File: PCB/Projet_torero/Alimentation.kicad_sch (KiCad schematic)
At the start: 21 parts, among them IC501 MP1475SGJ-P, J202 Conn_02x02_Odd_Even, J501 Conn_01x02, U501 BU33SD5WG-TR

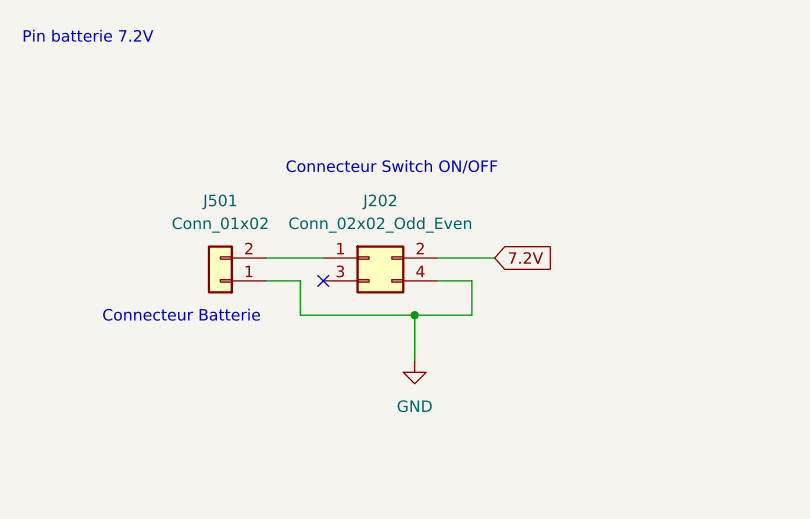
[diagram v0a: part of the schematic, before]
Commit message: Ajout Switch ON/OFF sur carte
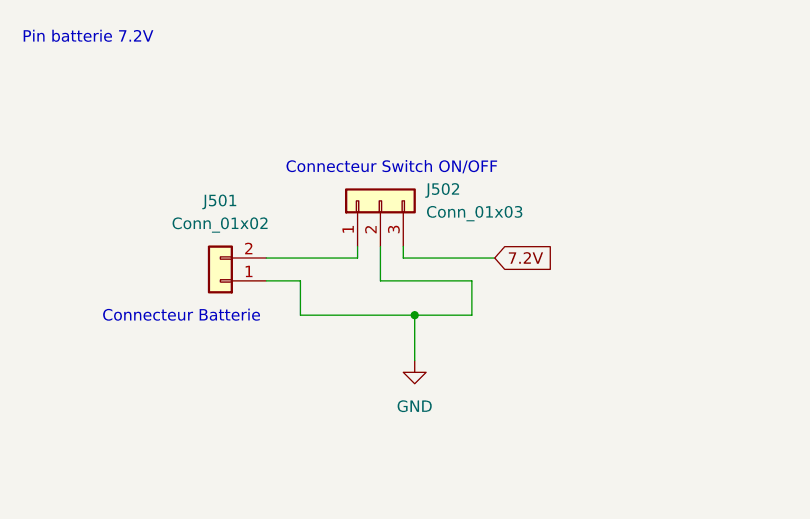
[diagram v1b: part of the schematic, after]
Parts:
- removed J202: Conn_02x02_Odd_Even, symbol Connector_Generic:Conn_02x02_Odd_Even
- added J502: Conn_01x03, symbol Connector_Generic:Conn_01x03
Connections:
- net 7.2V: now also J502.3 (Pin_3)
- net GND: now also J502.2 (Pin_2)
- net at J501.2 (Pin_2): now also J502.1 (Pin_1)
- no-connect marks 1 -> 0
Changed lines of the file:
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@@
 		(color 0 0 0 0)
 	)
-	(no_connect
-		(at 46.99 40.64)
-	)
 	(polyline
 		(pts
@@
 	(wire
 		(pts
+			(xy 50.8 38.1) (xy 50.8 36.83)
+		)
+		(stroke
+			(width 0)
+			(type default)
+		)
+	)
+	(wire
+		(pts
 			(xy 127 156.21) (xy 127 161.29)
 		)
@@
 	(wire
 		(pts
-			(xy 59.69 40.64) (xy 63.5 40.64)
-		)
-		(stroke
-			(width 0)
-			(type default)
-		)
-	)
-	(wire
-		(pts
-			(xy 59.69 38.1) (xy 66.04 38.1)
-		)
-		(stroke
-			(width 0)
-			(type default)
-		)
-	)
-	(wire
-		(pts
 			(xy 115.57 153.67) (xy 115.57 156.21)
 		)
@@
 	(wire
 		(pts
-			(xy 40.64 38.1) (xy 46.99 38.1)
+			(xy 40.64 38.1) (xy 50.8 38.1)
 		)
 		(stroke
@@
 	(wire
 		(pts
+			(xy 53.34 40.64) (xy 63.5 40.64)
+		)
+		(stroke
+			(width 0)
+			(type default)
+		)
+	)
+	(wire
+		(pts
 			(xy 205.74 123.19) (xy 207.01 123.19)
 		)
@@
 		)
 	)
+	(wire
+		(pts
+			(xy 55.88 38.1) (xy 66.04 38.1)
+		)
+		(stroke
+			(width 0)
+			(type default)
+		)
+	)
 	(polyline
 		(pts
@@
 	(wire
 		(pts
+			(xy 55.88 36.83) (xy 55.88 38.1)
+		)
+		(stroke
+			(width 0)
+			(type default)
+		)
+	)
+	(wire
+		(pts
 			(xy 71.12 147.32) (xy 71.12 152.4)
+		)
+		(stroke
+			(width 0)
+			(type default)
+		)
+	)
+	(wire
+		(pts
+			(xy 53.34 36.83) (xy 53.34 40.64)
 		)
 		(stroke
@@
 	)
 	(symbol
-		(lib_id "Connector_Generic:Conn_02x02_Odd_Even")
-		(at 52.07 38.1 0)
+		(lib_id "Connector_Generic:Conn_01x03")
+		(at 53.34 31.75 90)
 		(unit 1)
 		(exclude_from_sim no)
@@
 		(dnp no)
 		(fields_autoplaced yes)
-		(property "Reference" "J202"
+		(property "Reference" "J502"
+			(at 58.42 30.4799 90)
+			(effects
+				(font
+					(size 1.27 1.27)
+				)
+				(justify right)
+			)
+		)
+		(property "Value" "Conn_01x03"
+			(at 58.42 33.0199 90)
+			(effects
+				(font
+					(size 1.27 1.27)
+				)
+				(justify right)
+			)
+		)
+		(property "Footprint" ""
 			(at 53.34 31.75 0)
 			(effects
@@
 					(size 1.27 1.27)
 				)
-			)
-		)
-		(property "Value" "Conn_02x02_Odd_Even"
-			(at 53.34 34.29 0)
-			(effects
-				(font
-					(size 1.27 1.27)
-				)
-			)
-		)
-		(property "Footprint" ""
-			(at 52.07 38.1 0)
-			(effects
-				(font
-					(size 1.27 1.27)
-				)
 				(hide yes)
 			)
 		)
 		(property "Datasheet" "~"
-			(at 52.07 38.1 0)
-			(effects
-				(font
-					(size 1.27 1.27)
-				)
-				(hide yes)
-			)
-		)
-		(property "Description" "Generic connector, double row, 02x02, odd/even pin numbering scheme (row 1 odd numbers, row 2 even numbers), script generated (kicad-library-utils/schlib/autogen/connector/)"
-			(at 52.07 38.1 0)
-			(effects
-				(font
-					(size 1.27 1.27)
-				)
-				(hide yes)
-			)
+			(at 53.34 31.75 0)
+			(effects
+				(font
+					(size 1.27 1.27)
+				)
+				(hide yes)
+			)
+		)
+		(property "Description" "Generic connector, single row, 01x03, script generated (kicad-library-utils/schlib/autogen/connector/)"
+			(at 53.34 31.75 0)
+			(effects
+				(font
+					(size 1.27 1.27)
+				)
+				(hide yes)
+			)
+		)
+		(pin "1"
+		)
+		(pin "2"
 		)
 		(pin "3"
-		)
-		(pin "4"
-		)
-		(pin "2"
-		)
-		(pin "1"
 		)
 		(instances
 			(project ""
 				(path "/04e1eb47-a2c4-462b-bef7-377d9515a2c0/b3b2826c-2e3c-42fe-bcd6-22fcd6249c25"
-					(reference "J202")
+					(reference "J502")
 					(unit 1)
 				)

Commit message: Nouvelle version avec Empreinte correcte
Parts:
- J502: footprint (none) -> Connector_JST:JST_XH_S3B-XH-A_1x03_P2.50mm_Horizontal
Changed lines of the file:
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@@
 			)
 		)
-		(property "Footprint" ""
+		(property "Footprint" "Connector_JST:JST_XH_S3B-XH-A_1x03_P2.50mm_Horizontal"
 			(at 53.34 31.75 0)
 			(effects

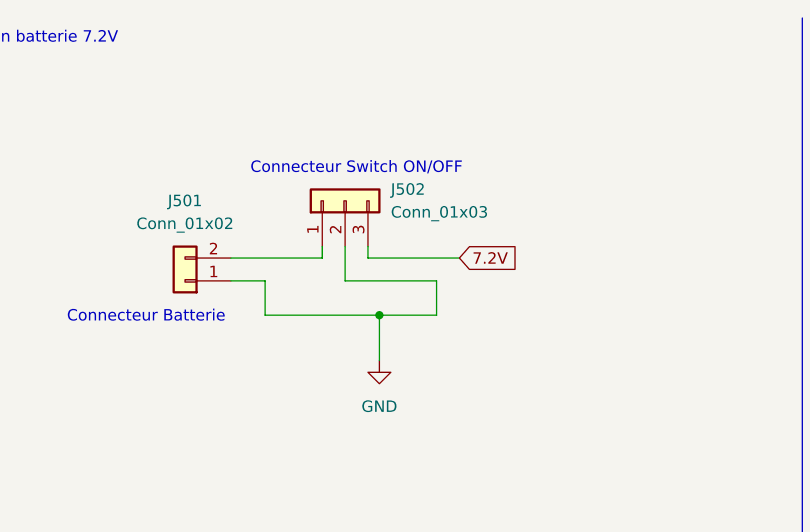
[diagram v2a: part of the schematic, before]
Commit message: Placement des composant "terminé"
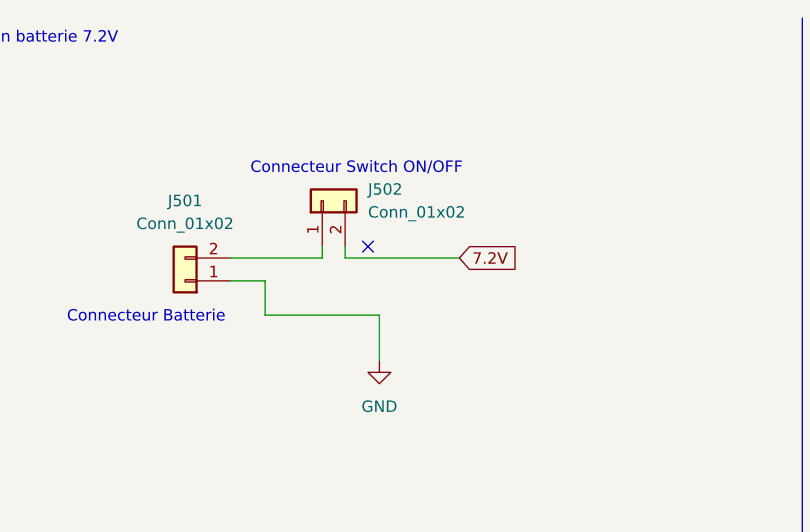
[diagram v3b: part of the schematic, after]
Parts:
- removed J502: Conn_01x03, Connector_JST:JST_XH_S3B-XH-A_1x03_P2.50mm_Horizontal, symbol Connector_Generic:Conn_01x03
- added J502: Conn_01x02, Connector_JST:JST_XH_S2B-XH-A_1x02_P2.50mm_Horizontal, symbol Connector_Generic:Conn_01x02
- C501: footprint Capacitor_SMD:C_0805_2012Metric_Pad1.18x1.45mm_HandSolder -> Capacitor_SMD:C_0805_2012Metric
- C504: footprint Capacitor_SMD:C_0603_1608Metric_Pad1.08x0.95mm_HandSolder -> Capacitor_SMD:C_0603_1608Metric
- L501: footprint Inductor_SMD:L_0603_1608Metric_Pad1.05x0.95mm_HandSolder -> Inductor_SMD:L_Wuerth_WE-TPC-3816
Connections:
- net 7.2V: now also J502.2 (Pin_2)
- net at J501.2 (Pin_2): now also J502.1 (Pin_1)
- no-connect marks 0 -> 1
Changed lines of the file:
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@@
 		(color 0 0 0 0)
 	)
-	(junction
-		(at 57.15 44.45)
-		(diameter 0)
-		(color 0 0 0 0)
+	(no_connect
+		(at 55.88 36.83)
+	)
+	(wire
+		(pts
+			(xy 66.04 38.1) (xy 53.34 38.1)
+		)
+		(stroke
+			(width 0)
+			(type default)
+		)
 	)
 	(polyline
@@
 	(wire
 		(pts
-			(xy 63.5 40.64) (xy 63.5 44.45)
-		)
-		(stroke
-			(width 0)
-			(type default)
-		)
-	)
-	(wire
-		(pts
 			(xy 203.2 120.65) (xy 203.2 127)
 		)
@@
 	(wire
 		(pts
-			(xy 63.5 44.45) (xy 57.15 44.45)
+			(xy 53.34 38.1) (xy 53.34 36.83)
 		)
 		(stroke
@@
 	(wire
 		(pts
-			(xy 53.34 40.64) (xy 63.5 40.64)
-		)
-		(stroke
-			(width 0)
-			(type default)
-		)
-	)
-	(wire
-		(pts
 			(xy 205.74 123.19) (xy 207.01 123.19)
 		)
@@
 		)
 	)
-	(wire
-		(pts
-			(xy 55.88 38.1) (xy 66.04 38.1)
-		)
-		(stroke
-			(width 0)
-			(type default)
-		)
-	)
 	(polyline
 		(pts
@@
 	(wire
 		(pts
-			(xy 55.88 36.83) (xy 55.88 38.1)
-		)
-		(stroke
-			(width 0)
-			(type default)
-		)
-	)
-	(wire
-		(pts
 			(xy 71.12 147.32) (xy 71.12 152.4)
-		)
-		(stroke
-			(width 0)
-			(type default)
-		)
-	)
-	(wire
-		(pts
-			(xy 53.34 36.83) (xy 53.34 40.64)
 		)
 		(stroke
@@
 			)
 		)
-		(property "Footprint" "Capacitor_SMD:C_0805_2012Metric_Pad1.18x1.45mm_HandSolder"
+		(property "Footprint" "Capacitor_SMD:C_0805_2012Metric"
 			(at 46.99 148.59 0)
 			(effects
@@
 			)
 		)
-		(property "Footprint" "Inductor_SMD:L_0603_1608Metric_Pad1.05x0.95mm_HandSolder"
+		(property "Footprint" "Inductor_SMD:L_Wuerth_WE-TPC-3816"
 			(at 110.49 138.43 0)
 			(effects
@@
 	)
 	(symbol
-		(lib_id "Connector_Generic:Conn_01x03")
-		(at 53.34 31.75 90)
-		(unit 1)
-		(exclude_from_sim no)
-		(in_bom yes)
-		(on_board yes)
-		(dnp no)
-		(fields_autoplaced yes)
-		(property "Reference" "J502"
-			(at 58.42 30.4799 90)
-			(effects
-				(font
-					(size 1.27 1.27)
-				)
-				(justify right)
-			)
-		)
-		(property "Value" "Conn_01x03"
-			(at 58.42 33.0199 90)
-			(effects
-				(font
-					(size 1.27 1.27)
-				)
-				(justify right)
-			)
-		)
-		(property "Footprint" "Connector_JST:JST_XH_S3B-XH-A_1x03_P2.50mm_Horizontal"
-			(at 53.34 31.75 0)
-			(effects
-				(font
-					(size 1.27 1.27)
-				)
-				(hide yes)
-			)
-		)
-		(property "Datasheet" "~"
-			(at 53.34 31.75 0)
-			(effects
-				(font
-					(size 1.27 1.27)
-				)
-				(hide yes)
-			)
-		)
-		(property "Description" "Generic connector, single row, 01x03, script generated (kicad-library-utils/schlib/autogen/connector/)"
-			(at 53.34 31.75 0)
-			(effects
-				(font
-					(size 1.27 1.27)
-				)
-				(hide yes)
-			)
-		)
-		(pin "1"
-		)
-		(pin "2"
-		)
-		(pin "3"
-		)
-		(instances
-			(project ""
-				(path "/04e1eb47-a2c4-462b-bef7-377d9515a2c0/b3b2826c-2e3c-42fe-bcd6-22fcd6249c25"
-					(reference "J502")
-					(unit 1)
-				)
-			)
-		)
-	)
-	(symbol
 		(lib_id "power:GND")
 		(at 57.15 49.53 0)
@@
 	)
 	(symbol
+		(lib_id "Connector_Generic:Conn_01x02")
+		(at 50.8 31.75 90)
+		(unit 1)
+		(exclude_from_sim no)
+		(in_bom yes)
+		(on_board yes)
+		(dnp no)
+		(fields_autoplaced yes)
+		(property "Reference" "J502"
+			(at 55.88 30.4799 90)
+			(effects
+				(font
+					(size 1.27 1.27)
+				)
+				(justify right)
+			)
+		)
+		(property "Value" "Conn_01x02"
+			(at 55.88 33.0199 90)
+			(effects
+				(font
+					(size 1.27 1.27)
+				)
+				(justify right)
+			)
+		)
+		(property "Footprint" "Connector_JST:JST_XH_S2B-XH-A_1x02_P2.50mm_Horizontal"
+			(at 50.8 31.75 0)
+			(effects
+				(font
+					(size 1.27 1.27)
+				)
+				(hide yes)
+			)
+		)
+		(property "Datasheet" "~"
+			(at 50.8 31.75 0)
+			(effects
+				(font
+					(size 1.27 1.27)
+				)
+				(hide yes)
+			)
+		)
+		(property "Description" "Generic connector, single row, 01x02, script generated (kicad-library-utils/schlib/autogen/connector/)"
+			(at 50.8 31.75 0)
+			(effects
+				(font
+					(size 1.27 1.27)
+				)
+				(hide yes)
+			)
+		)
+		(pin "1"
+		)
+		(pin "2"
+		)
+		(instances
+			(project "Projet_torero"
+				(path "/04e1eb47-a2c4-462b-bef7-377d9515a2c0/b3b2826c-2e3c-42fe-bcd6-22fcd6249c25"
+					(reference "J502")
+					(unit 1)
+				)
+			)
+		)
+	)
+	(symbol
 		(lib_id "Device:R_Small")
 		(at 97.79 144.78 270)
@@
 			)
 		)
-		(property "Footprint" "Capacitor_SMD:C_0603_1608Metric_Pad1.08x0.95mm_HandSolder"
+		(property "Footprint" "Capacitor_SMD:C_0603_1608Metric"
 			(at 127 153.67 0)
 			(effects

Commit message: Correction suggestion prof
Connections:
- net Sortie Régulateur 5V: now reaches C503.2, IC501.3 (SW), L501.1
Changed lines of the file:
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@@
+	(wire
+		(pts
+			(xy 128.27 40.64) (xy 132.08 40.64)
+		)
+		(stroke
+			(width 0)
+			(type default)
+		)
+	)
+	(wire
+		(pts
+			(xy 255.27 120.65) (xy 259.08 120.65)
+		)
+		(stroke
+			(width 0)
+			(type default)
+		)
+	)
+	(wire
+		(pts
+			(xy 46.99 132.08) (xy 71.12 132.08)
+		)
+		(stroke
+			(width 0)
+			(type default)
+		)
+	)
+	(wire
+		(pts
+			(xy 41.91 132.08) (xy 46.99 132.08)
+		)
+		(stroke
+			(width 0)
+			(type default)
+		)
+	)
+	(wire
+		(pts
+			(xy 247.65 120.65) (xy 255.27 120.65)
+		)
+		(stroke
+			(width 0)
+			(type default)
+		)
+	)
+	(wire
+		(pts
+			(xy 93.98 144.78) (xy 95.25 144.78)
+		)
+		(stroke
+			(width 0)
+			(type default)
+		)
+	)
+	(wire
+		(pts
+			(xy 128.27 30.48) (xy 128.27 25.4)
+		)
+		(stroke
+			(width 0)
+			(type default)
+		)
+	)
+	(wire
+		(pts
+			(xy 203.2 120.65) (xy 205.74 120.65)
+		)
+		(stroke
+			(width 0)
+			(type default)
+		)
+	)
+	(wire
+		(pts
+			(xy 59.69 151.13) (xy 59.69 154.94)
+		)
+		(stroke
+			(width 0)
+			(type default)
+		)
+	)
+	(wire
+		(pts
+			(xy 53.34 38.1) (xy 53.34 36.83)
+		)
+		(stroke
+			(width 0)
+			(type default)
+		)
+	)
+	(wire
+		(pts
+			(xy 227.33 138.43) (xy 227.33 139.7)
+		)
+		(stroke
+			(width 0)
+			(type default)
+		)
+	)
+	(wire
+		(pts
+			(xy 44.45 40.64) (xy 44.45 44.45)
+		)
+		(stroke
+			(width 0)
+			(type default)
+		)
+	)
+	(wire
+		(pts
+			(xy 71.12 152.4) (xy 64.77 152.4)
+		)
+		(stroke
+			(width 0)
+			(type default)
+		)
+	)
+	(wire
+		(pts
+			(xy 50.8 38.1) (xy 50.8 36.83)
+		)
+		(stroke
+			(width 0)
+			(type default)
+		)
+	)
+	(wire
+		(pts
+			(xy 127 156.21) (xy 127 161.29)
+		)
+		(stroke
+			(width 0)
+			(type default)
+		)
+	)
+	(wire
+		(pts
+			(xy 64.77 151.13) (xy 64.77 152.4)
+		)
+		(stroke
+			(width 0)
+			(type default)
+		)
+	)
+	(wire
+		(pts
+			(xy 205.74 120.65) (xy 205.74 123.19)
+		)
+		(stroke
+			(width 0)
+			(type default)
+		)
+	)
 	(wire
 		(pts
 			(xy 93.98 138.43) (xy 102.87 138.43)
-		)
-		(stroke
-			(width 0)
-			(type default)
-		)
-	)
-	(wire
-		(pts
-			(xy 128.27 40.64) (xy 132.08 40.64)
-		)
-		(stroke
-			(width 0)
-			(type default)
-		)
-	)
-	(wire
-		(pts
-			(xy 255.27 120.65) (xy 259.08 120.65)
-		)
-		(stroke
-			(width 0)
-			(type default)
-		)
-	)
-	(wire
-		(pts
-			(xy 46.99 132.08) (xy 71.12 132.08)
-		)
-		(stroke
-			(width 0)
-			(type default)
-		)
-	)
-	(wire
-		(pts
-			(xy 41.91 132.08) (xy 46.99 132.08)
-		)
-		(stroke
-			(width 0)
-			(type default)
-		)
-	)
-	(wire
-		(pts
-			(xy 247.65 120.65) (xy 255.27 120.65)
-		)
-		(stroke
-			(width 0)
-			(type default)
-		)
-	)
-	(wire
-		(pts
-			(xy 93.98 144.78) (xy 95.25 144.78)
-		)
-		(stroke
-			(width 0)
-			(type default)
-		)
-	)
-	(wire
-		(pts
-			(xy 128.27 30.48) (xy 128.27 25.4)
-		)
-		(stroke
-			(width 0)
-			(type default)
-		)
-	)
-	(wire
-		(pts
-			(xy 203.2 120.65) (xy 205.74 120.65)
-		)
-		(stroke
-			(width 0)
-			(type default)
-		)
-	)
-	(wire
-		(pts
-			(xy 59.69 151.13) (xy 59.69 154.94)
-		)
-		(stroke
-			(width 0)
-			(type default)
-		)
-	)
-	(wire
-		(pts
-			(xy 53.34 38.1) (xy 53.34 36.83)
-		)
-		(stroke
-			(width 0)
-			(type default)
-		)
-	)
-	(wire
-		(pts
-			(xy 227.33 138.43) (xy 227.33 139.7)
-		)
-		(stroke
-			(width 0)
-			(type default)
-		)
-	)
-	(wire
-		(pts
-			(xy 44.45 40.64) (xy 44.45 44.45)
-		)
-		(stroke
-			(width 0)
-			(type default)
-		)
-	)
-	(wire
-		(pts
-			(xy 71.12 152.4) (xy 64.77 152.4)
-		)
-		(stroke
-			(width 0)
-			(type default)
-		)
-	)
-	(wire
-		(pts
-			(xy 50.8 38.1) (xy 50.8 36.83)
-		)
-		(stroke
-			(width 0)
-			(type default)
-		)
-	)
-	(wire
-		(pts
-			(xy 127 156.21) (xy 127 161.29)
-		)
-		(stroke
-			(width 0)
-			(type default)
-		)
-	)
-	(wire
-		(pts
-			(xy 64.77 151.13) (xy 64.77 152.4)
-		)
-		(stroke
-			(width 0)
-			(type default)
-		)
-	)
-	(wire
-		(pts
-			(xy 205.74 120.65) (xy 205.74 123.19)
 		)
 		(stroke
@@
 				(size 1.27 1.27)
 			)
+		)
+	)
+	(label "Sortie Régulateur 5V"
+		(at 93.98 138.43 0)
+		(fields_autoplaced yes)
+		(effects
+			(font
+				(size 1.27 1.27)
+			)
+			(justify left bottom)
 		)
 	)
@@
 		(dnp no)
 		(property "Reference" "L501"
-			(at 107.95 139.954 90)
+			(at 112.014 134.366 90)
 			(effects
 				(font
@@
 		)
 		(property "Value" "4u7"
-			(at 108.204 141.732 90)
-			(effects
-				(font
+			(at 112.268 136.144 90)
+			(effects
+				(font
